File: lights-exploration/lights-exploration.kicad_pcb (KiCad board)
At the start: 2 copper layers, 86.8 x 90 mm, 2 parts

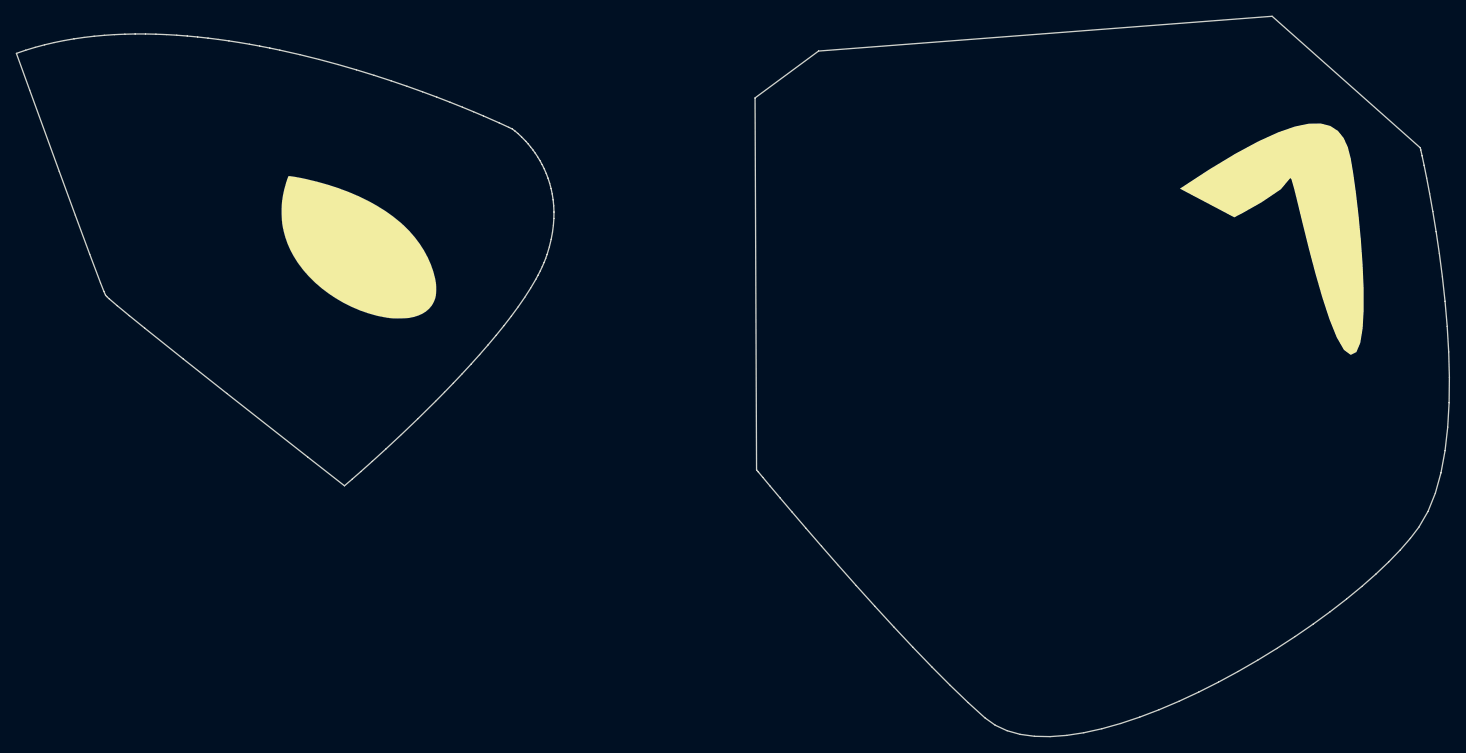
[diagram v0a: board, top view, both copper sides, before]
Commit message: Nested cuts test
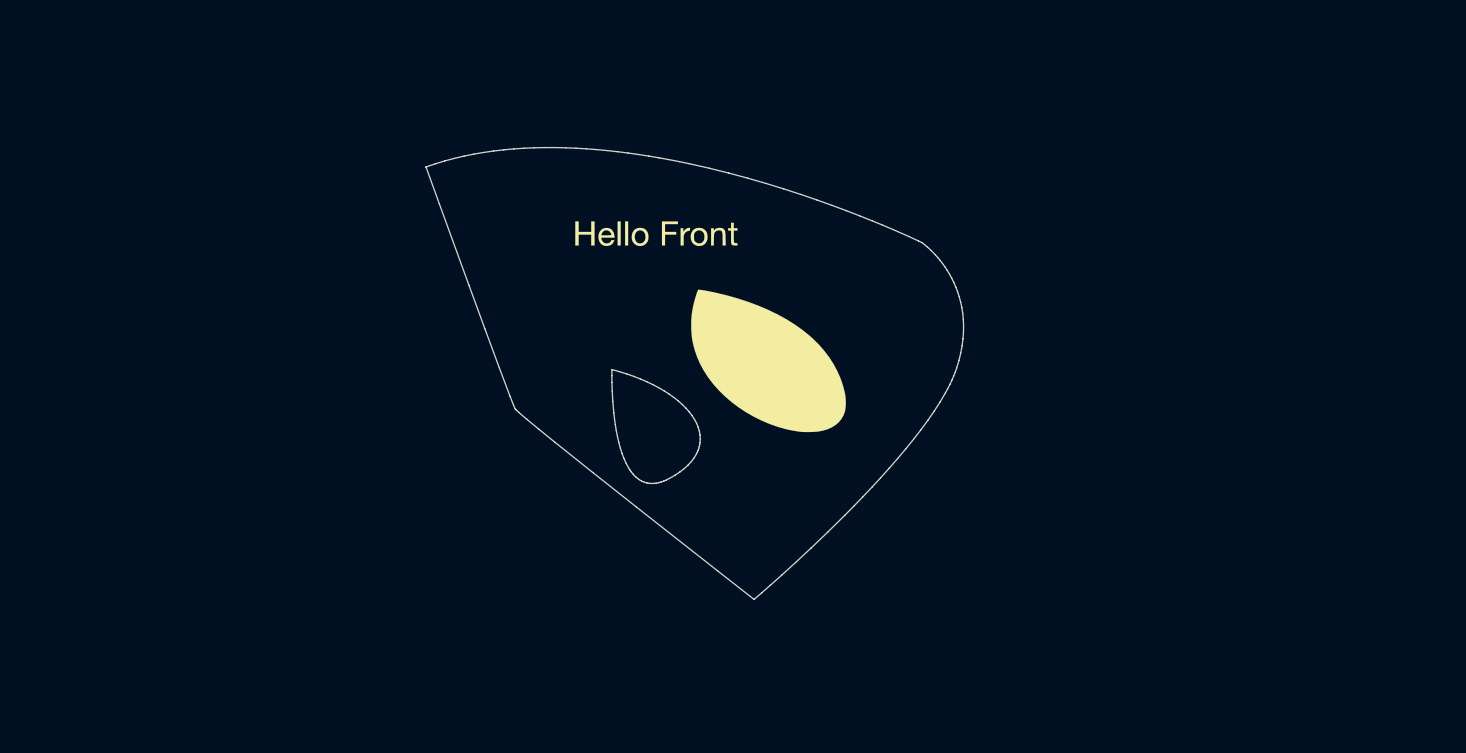
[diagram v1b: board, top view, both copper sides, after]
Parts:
- removed svg2mod: G***, exploration-1:exploration-1
- moved ? 53.1 mm to (152.7, 72.7)
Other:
- board size 86.8 x 90 mm -> 67.2 x 56.5 mm
